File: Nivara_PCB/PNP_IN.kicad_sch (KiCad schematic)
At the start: 0 parts

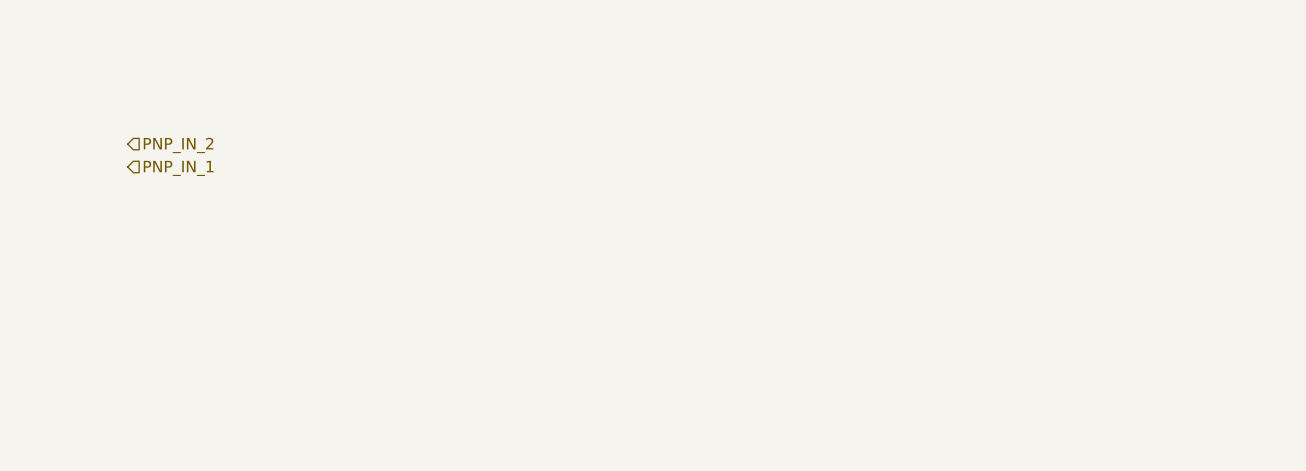
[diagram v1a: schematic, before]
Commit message: Añadido de funciones NPN/PNP
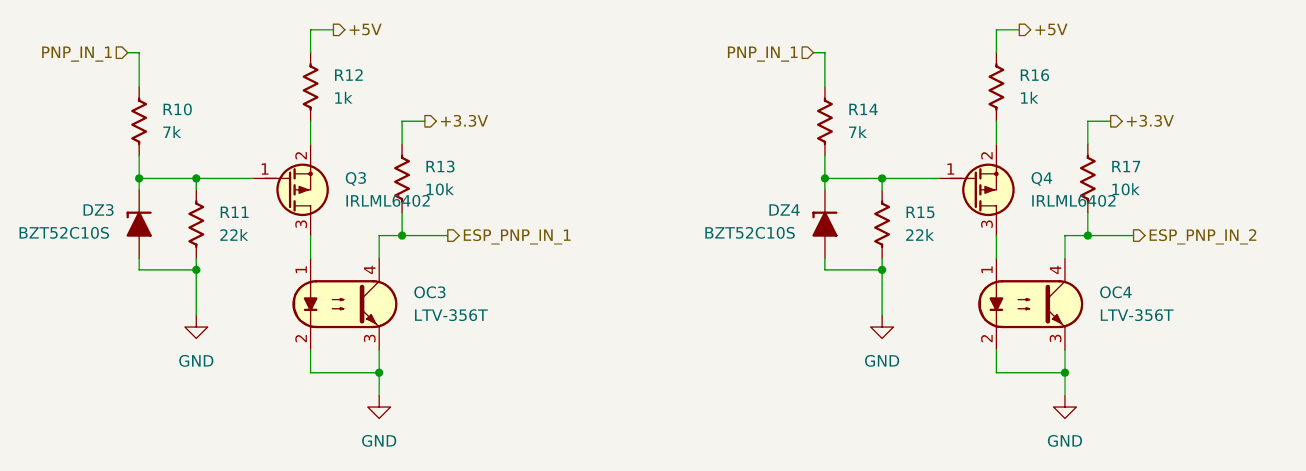
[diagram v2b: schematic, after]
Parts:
- added DZ3, DZ4: BZT52C10S, PCM_Diode_SMD_AKL:D_SOD-323, symbol PCM_Diode_Zener_AKL:BZT52C10S
- added OC3, OC4: LTV-356T, PCM_Package_SO_AKL:SO-4_4.4x3.9mm_P2.54mm, symbol PCM_Optocoupler_AKL:LTV-356T
- added Q3, Q4: IRLML6402, PCM_Package_TO_SOT_SMD_AKL:SOT-23, symbol PCM_Transistor_MOSFET_AKL:IRLML6402
- added R10, R14: 7k, PCM_Resistor_SMD_AKL:R_0603_1608Metric, symbol PCM_Resistor_US_AKL:R_0603
- added R11, R15: 22k, PCM_Resistor_SMD_AKL:R_0603_1608Metric, symbol PCM_Resistor_US_AKL:R_0603
- added R12, R16: 1k, PCM_Resistor_SMD_AKL:R_0603_1608Metric, symbol PCM_Resistor_US_AKL:R_0603
- added R13, R17: 10k, PCM_Resistor_SMD_AKL:R_0603_1608Metric, symbol PCM_Resistor_US_AKL:R_0603
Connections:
- net PNP_IN_1: now also R10.1, R14.1
- new net: DZ4.1 (K), Q4.1 (G), R14.2, R15.1
- new net: Q4.2 (S), R16.2
- new net: DZ3.1 (K), Q3.1 (G), R10.2, R11.1
- new net: OC4.1, Q4.3 (D)
- new net: OC3.1, Q3.3 (D)
- new net: Q3.2 (S), R12.2
- new net +3.3V: R13.1, R17.1
- new net +5V: R12.1, R16.1
- new net ESP_PNP_IN_1: OC3.4, R13.2
- new net ESP_PNP_IN_2: OC4.4, R17.2
- new net GND: DZ3.2 (A), DZ4.2 (A), OC3.2, OC3.3, OC4.2, OC4.3, R11.2, R15.2

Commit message: Cambios en el diseño del pcb
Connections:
- net PNP_IN_1: no longer R14.1
- new net PNP_IN_2: R14.1
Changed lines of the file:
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@@
 		)
 	)
-	(hierarchical_label "PNP_IN_1"
+	(hierarchical_label "PNP_IN_2"
 		(shape input)
 		(at 115.57 43.18 180)

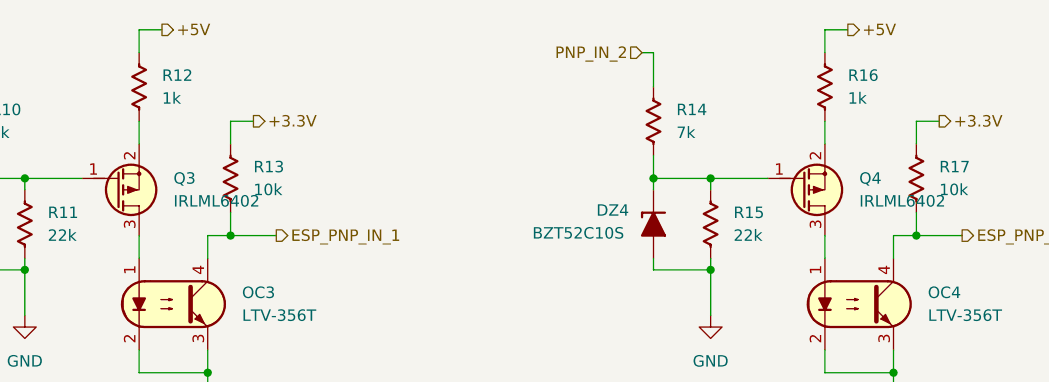
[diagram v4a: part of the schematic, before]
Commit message: Cambios en el esquema de NPN y PNP
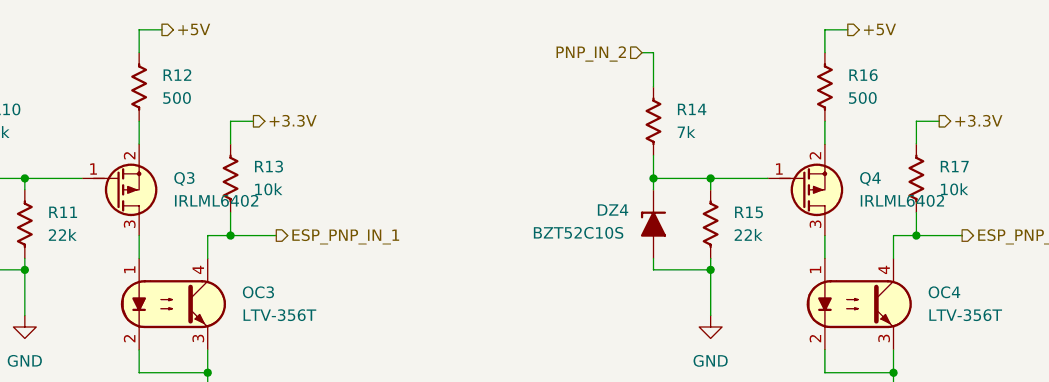
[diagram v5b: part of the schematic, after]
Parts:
- R12, R16: value 1k -> 500
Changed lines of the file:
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@@
 			)
 		)
-		(property "Value" "1k"
+		(property "Value" "500"
 			(at 138.43 48.2599 0)
 			(effects
@@
 			)
 		)
-		(property "Value" "1k"
+		(property "Value" "500"
 			(at 62.23 48.2599 0)
 			(effects

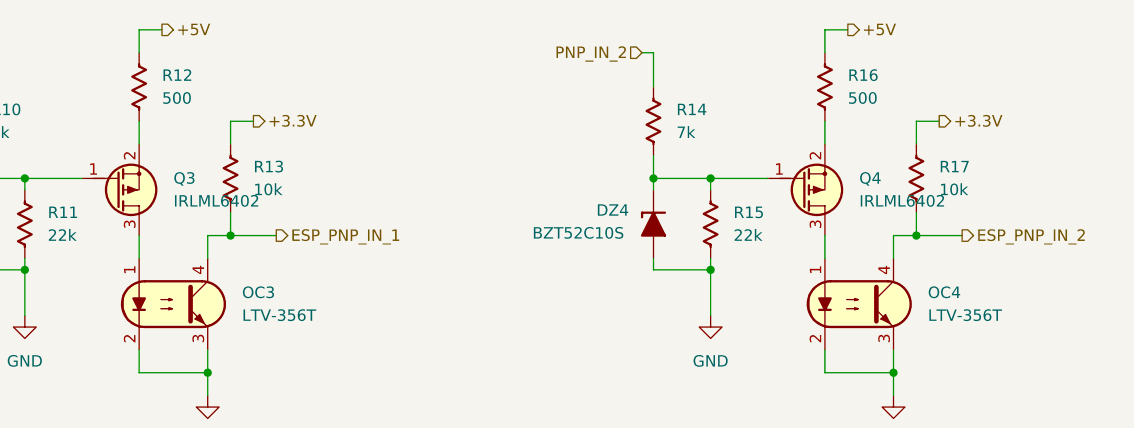
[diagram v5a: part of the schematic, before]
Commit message: Cambio de IntelliFet, porque los que tenían no estaban disponibles.
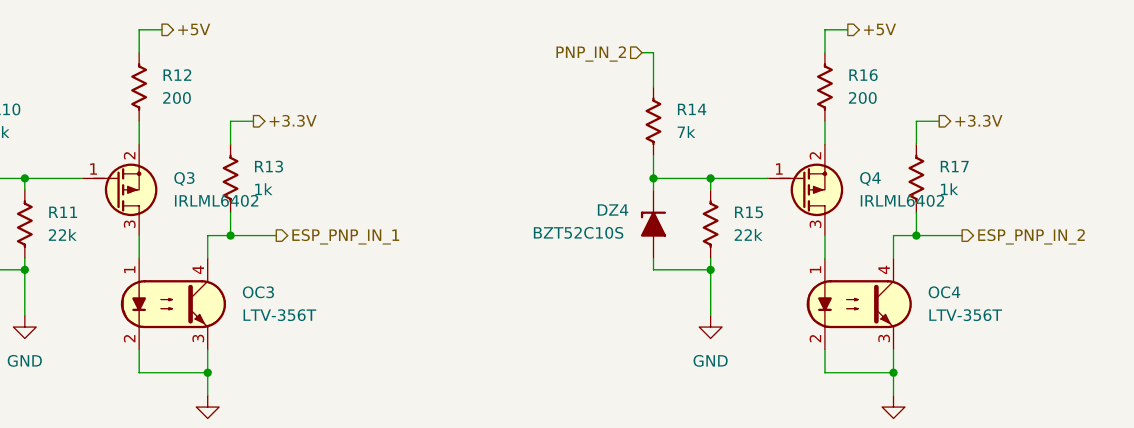
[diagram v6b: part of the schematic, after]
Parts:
- R12, R16: value 500 -> 200
- R13, R17: value 10k -> 1k
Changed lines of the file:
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@@
 			)
 		)
-		(property "Value" "10k"
+		(property "Value" "1k"
 			(at 148.59 58.4199 0)
 			(effects
@@
 			)
 		)
-		(property "Value" "500"
+		(property "Value" "200"
 			(at 138.43 48.2599 0)
 			(effects
@@
 			)
 		)
-		(property "Value" "10k"
+		(property "Value" "1k"
 			(at 72.39 58.4199 0)
 			(effects
@@
 			)
 		)
-		(property "Value" "500"
+		(property "Value" "200"
 			(at 62.23 48.2599 0)
 			(effects

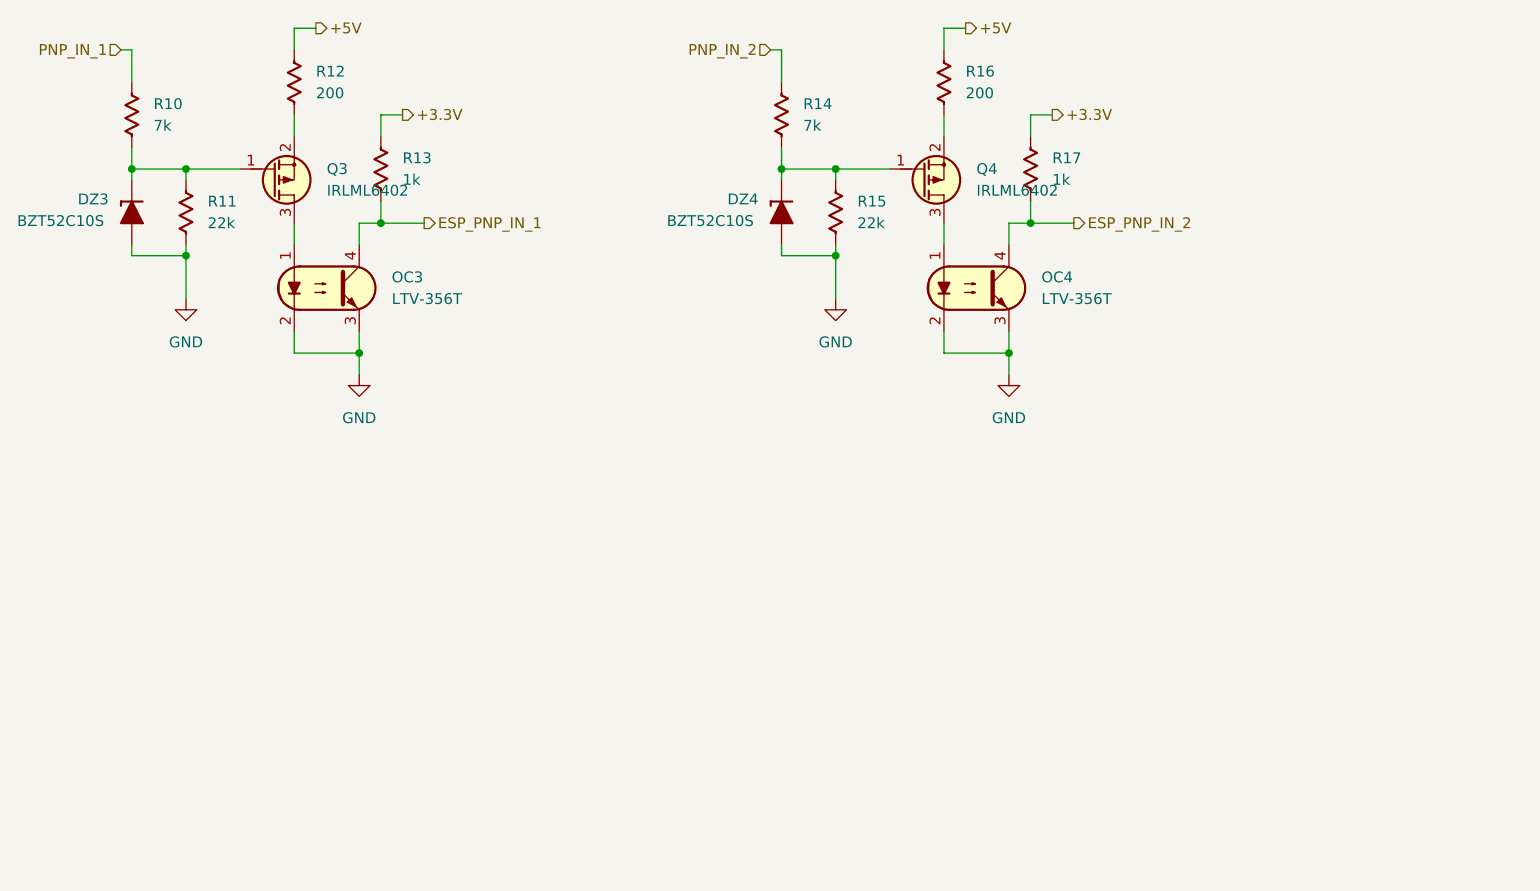
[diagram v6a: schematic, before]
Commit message: Cambios en las mediciones análogas.
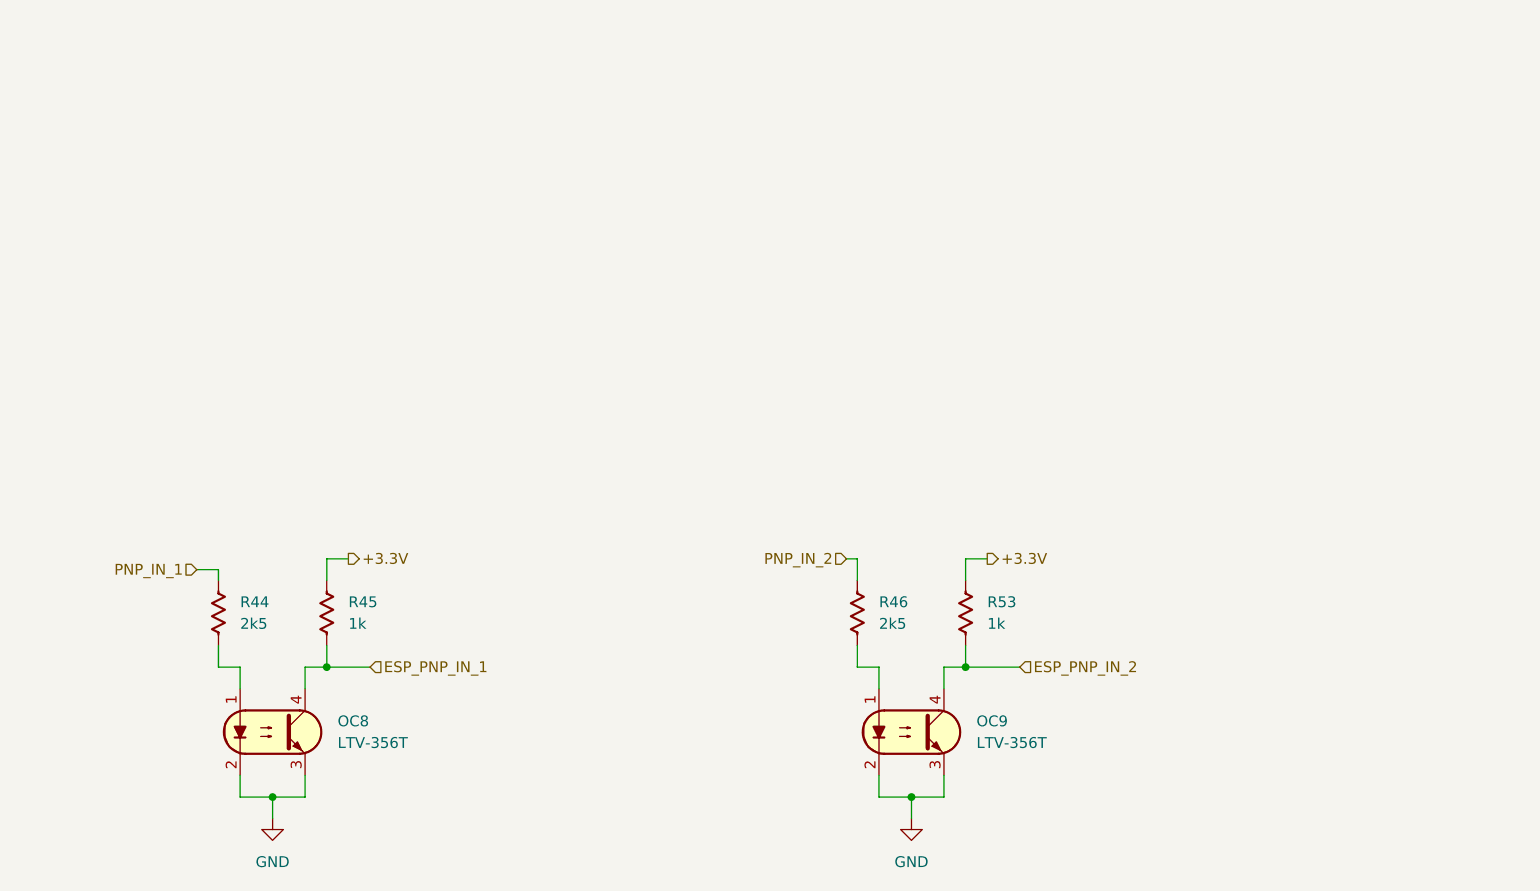
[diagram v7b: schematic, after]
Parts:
- removed DZ3, DZ4: BZT52C10S, PCM_Diode_SMD_AKL:D_SOD-323, symbol PCM_Diode_Zener_AKL:BZT52C10S
- removed OC3, OC4: LTV-356T, PCM_Package_SO_AKL:SO-4_4.4x3.9mm_P2.54mm, symbol PCM_Optocoupler_AKL:LTV-356T
- removed Q3, Q4: IRLML6402, PCM_Package_TO_SOT_SMD_AKL:SOT-23, symbol PCM_Transistor_MOSFET_AKL:IRLML6402
- removed R10, R14: 7k, PCM_Resistor_SMD_AKL:R_0603_1608Metric, symbol PCM_Resistor_US_AKL:R_0603
- removed R11, R15: 22k, PCM_Resistor_SMD_AKL:R_0603_1608Metric, symbol PCM_Resistor_US_AKL:R_0603
- removed R12, R16: 200, PCM_Resistor_SMD_AKL:R_0603_1608Metric, symbol PCM_Resistor_US_AKL:R_0603
- removed R13, R17: 1k, PCM_Resistor_SMD_AKL:R_0603_1608Metric, symbol PCM_Resistor_US_AKL:R_0603
- added OC8, OC9: LTV-356T, PCM_Package_SO_AKL:SO-4_4.4x3.9mm_P2.54mm, symbol PCM_Optocoupler_AKL:LTV-356T
- added R44, R46: 2k5, PCM_Resistor_SMD_AKL:R_0603_1608Metric, symbol PCM_Resistor_US_AKL:R_0603
- added R45, R53: 1k, PCM_Resistor_SMD_AKL:R_0603_1608Metric, symbol PCM_Resistor_US_AKL:R_0603
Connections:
- net +3.3V: now also R45.1, R53.1
- net ESP_PNP_IN_1: now also OC8.4, R45.2
- net ESP_PNP_IN_2: now also OC9.4, R53.2
- net GND: now also OC8.2, OC8.3, OC9.2, OC9.3
- net PNP_IN_1: now also R44.1
- net PNP_IN_2: now also R46.1
- new net: OC9.1, R46.2
- new net: OC8.1, R44.2

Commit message: Cambios en las salidas analogicas, ya que el ESP32 S3 no tiene DAC
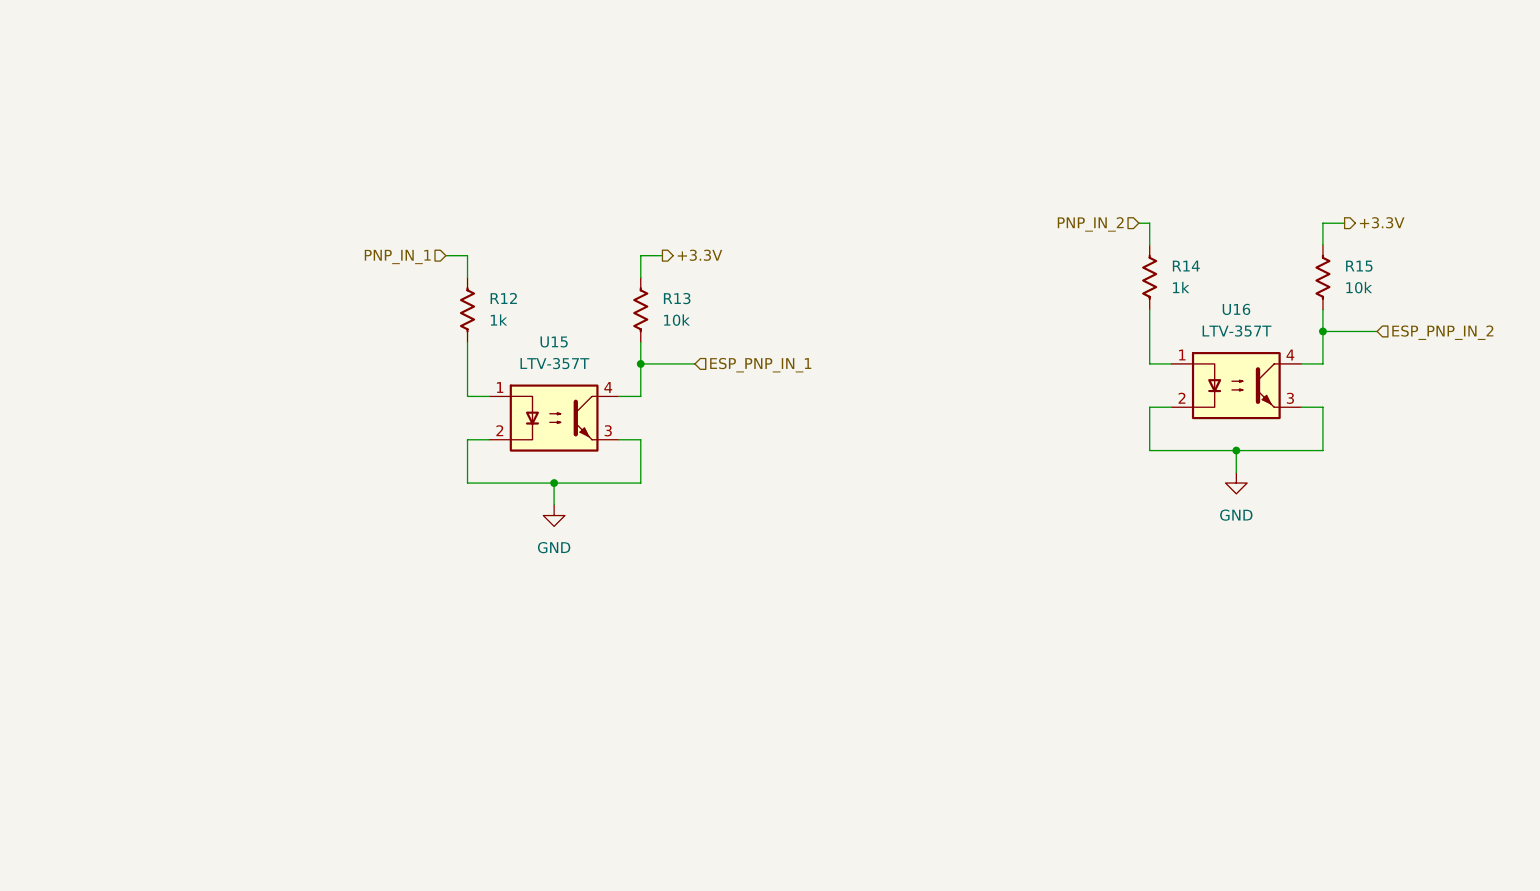
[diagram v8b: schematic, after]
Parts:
- removed OC8, OC9: LTV-356T, PCM_Package_SO_AKL:SO-4_4.4x3.9mm_P2.54mm, symbol PCM_Optocoupler_AKL:LTV-356T
- removed R44, R46: 2k5, PCM_Resistor_SMD_AKL:R_0603_1608Metric, symbol PCM_Resistor_US_AKL:R_0603
- removed R45, R53: 1k, PCM_Resistor_SMD_AKL:R_0603_1608Metric, symbol PCM_Resistor_US_AKL:R_0603
- added R12, R14: 1k, PCM_Resistor_SMD_AKL:R_0603_1608Metric, symbol PCM_Resistor_US_AKL:R_0603
- added R13, R15: 10k, PCM_Resistor_SMD_AKL:R_0603_1608Metric, symbol PCM_Resistor_US_AKL:R_0603
- added U15, U16: LTV-357T, Package_SO:SO-4_4.4x3.6mm_P2.54mm, symbol Isolator:LTV-357T
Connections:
- net +3.3V: now also R13.1, R15.1
- net ESP_PNP_IN_1: now also R13.2, U15.4
- net ESP_PNP_IN_2: now also R15.2, U16.4
- net GND: now also U15.2, U15.3, U16.2, U16.3
- net PNP_IN_1: now also R12.1
- net PNP_IN_2: now also R14.1
- new net: R12.2, U15.1
- new net: R14.2, U16.1
